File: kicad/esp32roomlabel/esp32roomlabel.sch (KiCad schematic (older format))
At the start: 11 parts, among them J1 BME280, J2 OLED, J3 LCD2004, J4 DS3231, J5 DHT22, J6 Switch1, J7 Switch2, J8 MISC, J9 LED, U1 NODEMCU ESP32

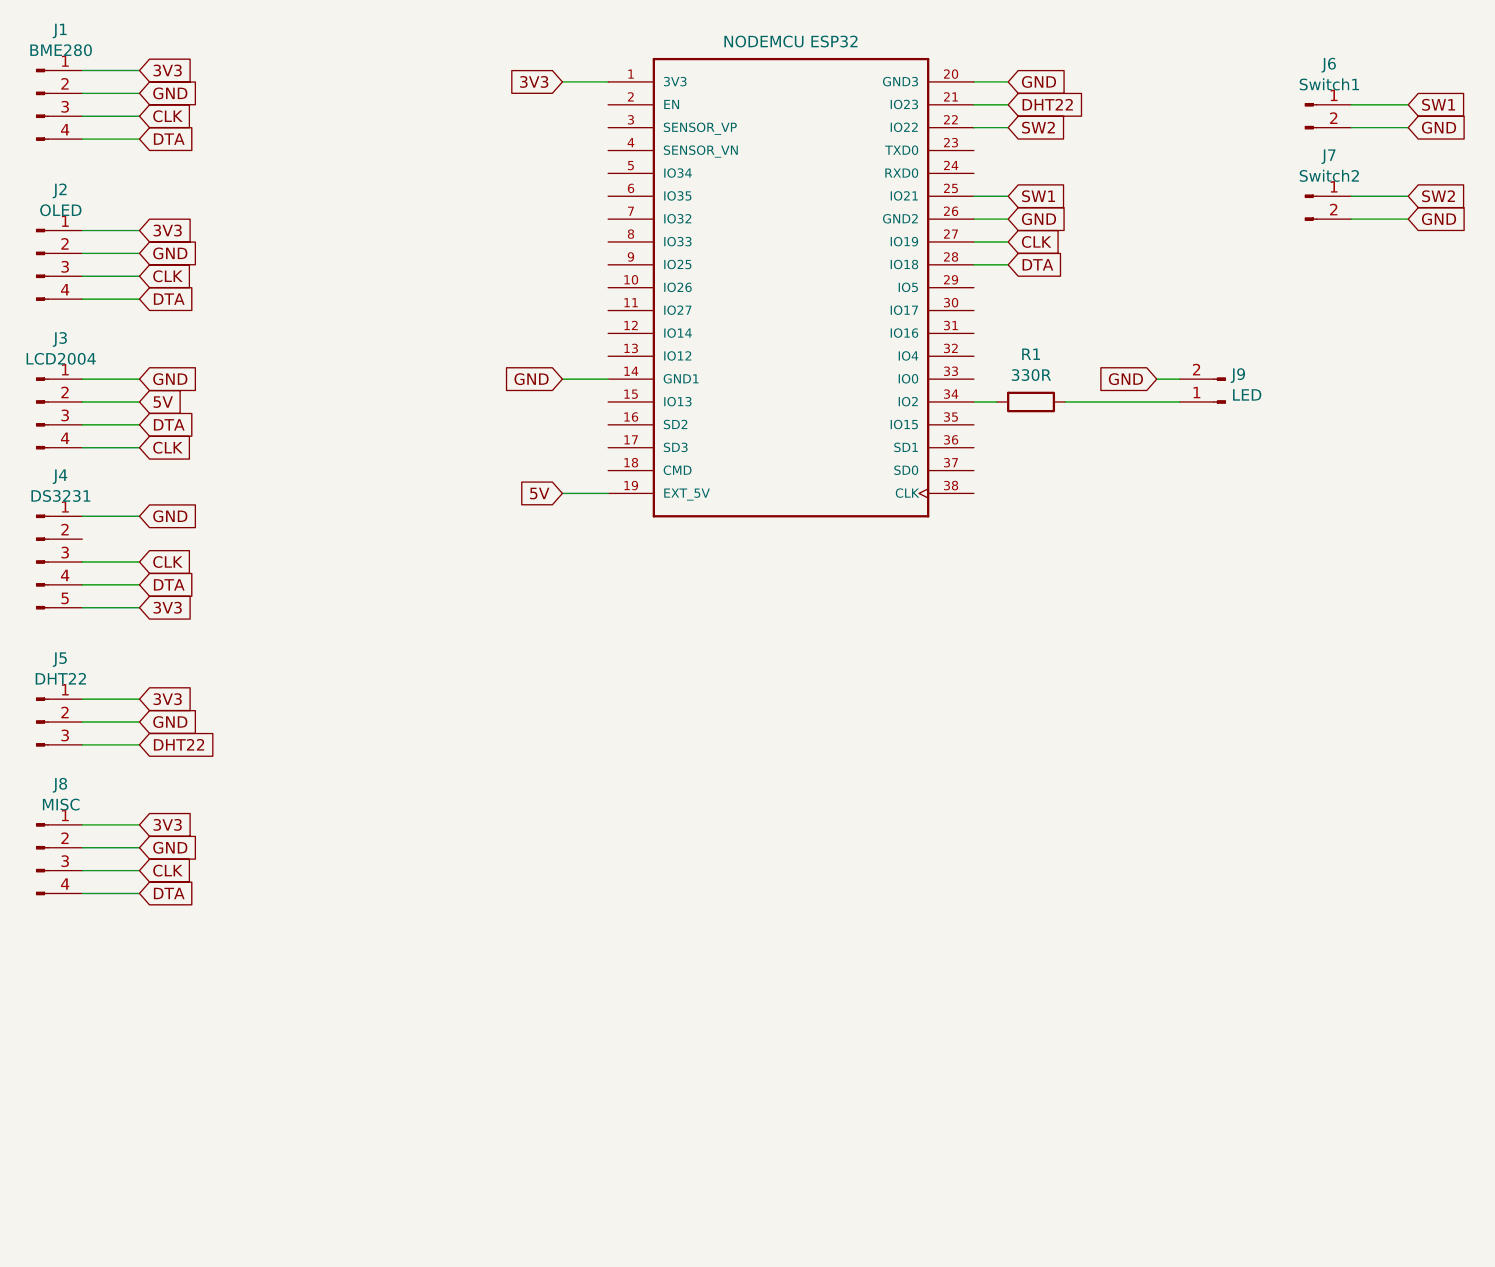
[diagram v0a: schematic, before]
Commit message: Updated PCB
Added GPIO and Analog pin header
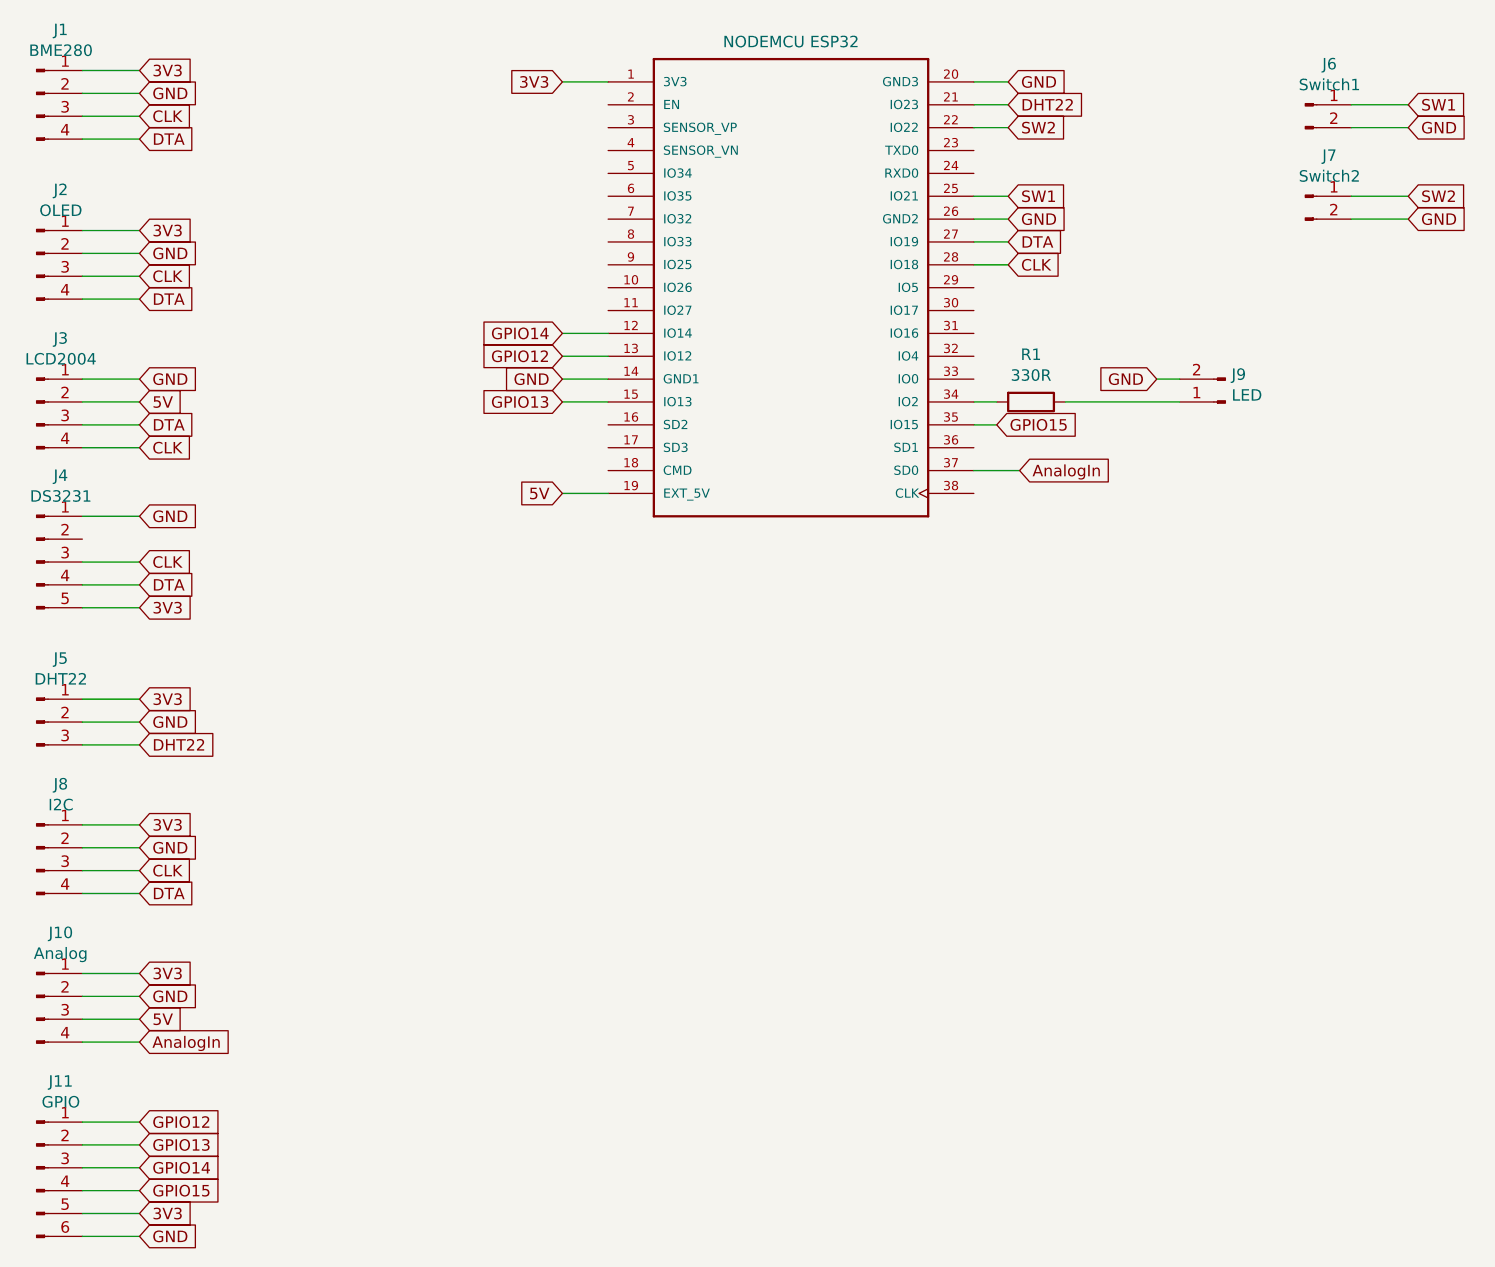
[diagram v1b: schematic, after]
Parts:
- added J10: Analog, Connector_PinHeader_2.54mm:PinHeader_1x04_P2.54mm_Vertical, symbol Connector:Conn_01x04_Male
- added J11: GPIO, Connector_PinHeader_2.54mm:PinHeader_1x06_P2.54mm_Vertical, symbol Connector:Conn_01x06_Male
- J8: value MISC -> I2C
- U1: footprint ESP32-DEVKITC-32D:MODULE_ESP32-DEVKITC-32D -> ESP32-DEVKIT:MODULE_ESP32-DEVKITC-32D
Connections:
- net 3V3: now also J10.1 (Pin_1), J11.5 (Pin_5)
- net 5V: now also J10.3 (Pin_3)
- net CLK: now also U1.28 (IO18); no longer U1.27 (IO19)
- net DTA: now also U1.27 (IO19); no longer U1.28 (IO18)
- net GND: now also J10.2 (Pin_2), J11.6 (Pin_6)
- net GPIO14: now reaches U1.12 (IO14)
- net GPIO14: now also J11.3 (Pin_3)
- net GPIO12: now reaches U1.13 (IO12)
- net GPIO12: now also J11.1 (Pin_1)
- net GPIO13: now reaches U1.15 (IO13)
- net GPIO13: now also J11.2 (Pin_2)
- net GPIO15: now reaches U1.35 (IO15)
- net GPIO15: now also J11.4 (Pin_4)
- net AnalogIn: now reaches U1.37 (SD0)
- net AnalogIn: now also J10.4 (Pin_4)
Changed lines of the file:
@@
 EESchema Schematic File Version 4
+LIBS:esp32roomlabel-cache
 EELAYER 26 0
 EELAYER END
@@
 F 0 "U1" H 4850 4467 50  0001 C CNN
 F 1 "NODEMCU ESP32" H 4850 4375 50  0000 C CNN
-F 2 "ESP32-DEVKITC-32D:MODULE_ESP32-DEVKITC-32D" H 4850 3300 50  0001 L BNN
+F 2 "ESP32-DEVKIT:MODULE_ESP32-DEVKITC-32D" H 4850 3300 50  0001 L BNN
 F 3 "Unavailable" H 4850 3300 50  0001 L BNN
 F 4 "Espressif Systems" H 4850 3300 50  0001 L BNN "Feld4"
@@
 Wire Wire Line
 	5650 3000 5800 3000
+Text GLabel 5800 3200 2    50   Input ~ 0
+CLK
 Text GLabel 5800 3100 2    50   Input ~ 0
-CLK
-Text GLabel 5800 3200 2    50   Input ~ 0
 DTA
 Wire Wire Line
@@
 P 1550 5750
 F 0 "J8" H 1656 6028 50  0000 C CNN
-F 1 "MISC" H 1656 5937 50  0000 C CNN
+F 1 "I2C" H 1656 5937 50  0000 C CNN
 F 2 "Connector_PinHeader_2.54mm:PinHeader_1x04_P2.54mm_Vertical" H 1550 5750 50  0001 C CNN
 F 3 "~" H 1550 5750 50  0001 C CNN
@@
 Wire Wire Line
 	3850 3700 4050 3700
+$Comp
+L Connector:Conn_01x04_Male J10
+U 1 1 5D7A29E7
+P 1550 6400
+F 0 "J10" H 1656 6678 50  0000 C CNN
+F 1 "Analog" H 1656 6587 50  0000 C CNN
+F 2 "Connector_PinHeader_2.54mm:PinHeader_1x04_P2.54mm_Vertical" H 1550 6400 50  0001 C CNN
+F 3 "~" H 1550 6400 50  0001 C CNN
+	1    1550 6400
+	1    0    0    -1
+$EndComp
+Text GLabel 2000 6300 2    50   Input ~ 0
+3V3
+Text GLabel 2000 6400 2    50   Input ~ 0
+GND
+Text GLabel 2000 6500 2    50   Input ~ 0
+5V
+Text GLabel 2000 6600 2    50   Input ~ 0
+AnalogIn
+Wire Wire Line
+	2000 6600 1750 6600
+Wire Wire Line
+	1750 6500 2000 6500
+Wire Wire Line
+	2000 6400 1750 6400
+Wire Wire Line
+	2000 6300 1750 6300
+Text GLabel 5850 4100 2    50   Input ~ 0
+AnalogIn
+Wire Wire Line
+	5650 4100 5850 4100
+Text GLabel 2000 7150 2    50   Input ~ 0
+GPIO14
+Text GLabel 2000 7250 2    50   Input ~ 0
+GPIO15
+Text GLabel 2000 7050 2    50   Input ~ 0
+GPIO13
+Text GLabel 5750 3900 2    50   Input ~ 0
+GPIO15
+Wire Wire Line
+	3850 3500 4050 3500
+Wire Wire Line
+	3850 3600 4050 3600
+Wire Wire Line
+	3850 3800 4050 3800
+Wire Wire Line
+	5650 3900 5750 3900
+$Comp
+L Connector:Conn_01x06_Male J11
+U 1 1 5D7A9346
+P 1550 7150
+F 0 "J11" H 1656 7528 50  0000 C CNN
+F 1 "GPIO" H 1656 7437 50  0000 C CNN
+F 2 "Connector_PinHeader_2.54mm:PinHeader_1x06_P2.54mm_Vertical" H 1550 7150 50  0001 C CNN
+F 3 "~" H 1550 7150 50  0001 C CNN
+	1    1550 7150
+	1    0    0    -1
+$EndComp
+Text GLabel 2000 6950 2    50   Input ~ 0
+GPIO12
+Text GLabel 3850 3600 0    50   Input ~ 0
+GPIO12
+Text GLabel 3850 3800 0    50   Input ~ 0
+GPIO13
+Text GLabel 3850 3500 0    50   Input ~ 0
+GPIO14
+Text GLabel 2000 7350 2    50   Input ~ 0
+3V3
+Text GLabel 2000 7450 2    50   Input ~ 0
+GND
+Wire Wire Line
+	1750 7450 2000 7450
+Wire Wire Line
+	1750 7350 2000 7350
+Wire Wire Line
+	1750 7250 2000 7250
+Wire Wire Line
+	1750 7150 2000 7150
+Wire Wire Line
+	1750 7050 2000 7050
+Wire Wire Line
+	1750 6950 2000 6950
 $EndSCHEMATC
